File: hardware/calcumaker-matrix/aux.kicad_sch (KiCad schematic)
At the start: 1 part, among them J2 OLED 128x32 (DNP)

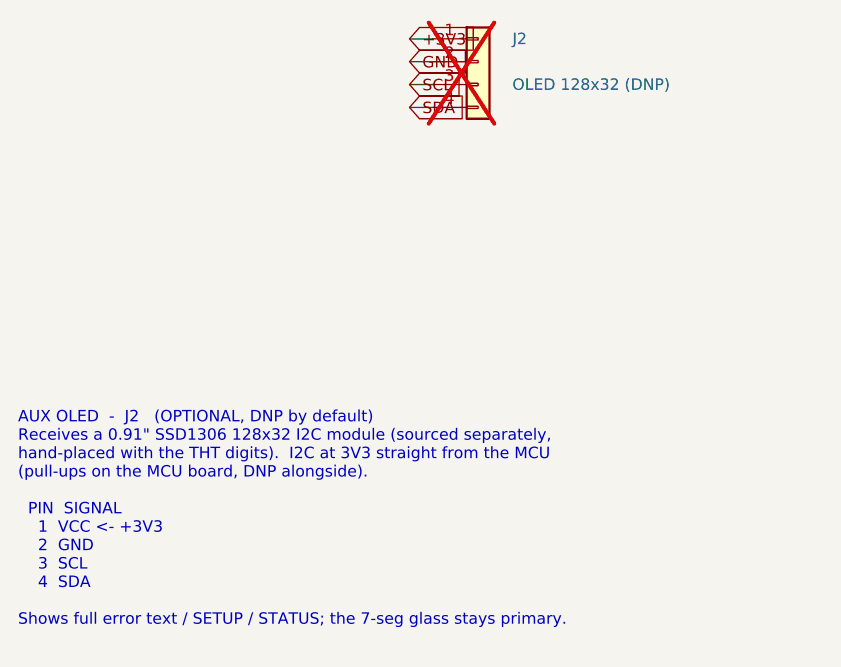
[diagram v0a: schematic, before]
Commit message: hardware: unified SPI display-module interface + RGB dot-matrix board
Make the display a swappable module on ONE technology-agnostic connector
(mirrors the keyboard-G0 pattern): the MCU board speaks a single SPI
"display intent" bus and each display board carries its own MCU that
renders locally. Two interchangeable modules on the same 12-pin FFC.

- calcumaker-matrix (NEW): full-color RGB dot matrix, 96x24 = 2304x 1mm
  XL-1010RGBC-2812B-S (C51900942) driven by an RP2040 (PIO). Nested
  multi-channel: led_cluster (8x8) x12 -> led_row (768px chain) x3.
  Dedicated VSYS LED-power inlet keeps amps off the signal FFC. Authored
  the 1mm 1010 footprint; RP2040/flash/shifter symbols are stock.
- calcumaker-display (7-seg): retrofit to a smart module -- added an
  STM32G031 SPI slave, and moved the 5V boost (TPS61022) + 74HCT125
  shifter off the MCU board onto it. Interconnect reworked CLK/DIN -> SPI.
- calcumaker-mcu: DisplayIF simplified to the unified SPI connector +
  a 2-pin VSYS outlet for the matrix LED rail.

Unified pinout (mcu J3 / display J1 / matrix J1): VSYS,VSYS,GND,GND,+3V3,
SPI_SCLK,SPI_MOSI,SPI_CS,DISP_IRQ,DISP_NRST,DISP_BOOT,GND.

All boards generate + check clean (mcu 46 / keyboard 179 / display 77 /
matrix 2339, no dup refs). Docs (PARTS.md, DESIGN.md, Makefile) updated.
Firmware is deferred; the SPI contract is documented so it is unblocked.

Co-Authored-By: Claude Opus 4.8 (1M context) <noreply@anthropic.com>
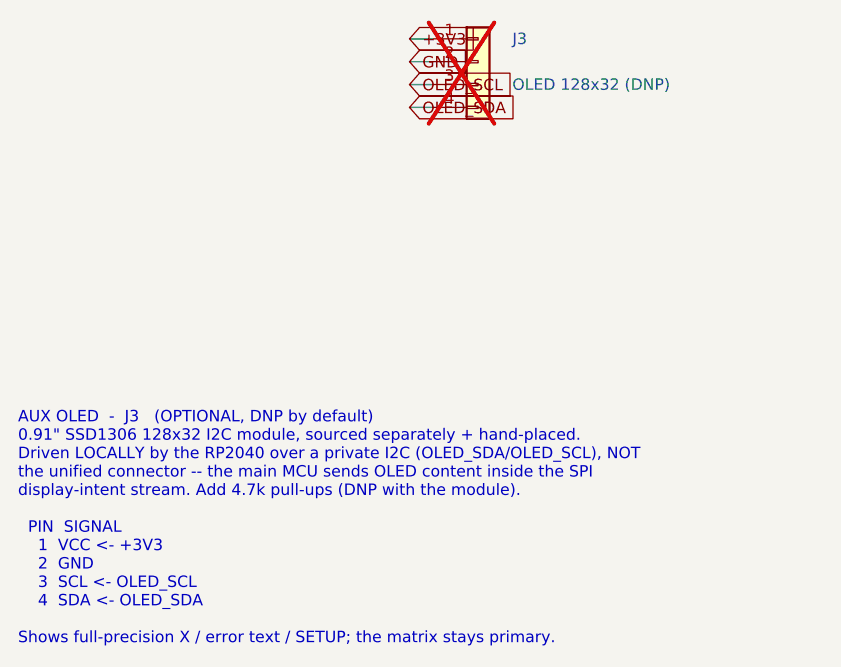
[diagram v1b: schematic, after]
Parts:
- removed J2: OLED 128x32 (DNP), Connector_PinHeader_2.54mm:PinHeader_1x04_P2.54mm_Vertical, symbol Connector_Generic:Conn_01x04
- added J3: OLED 128x32 (DNP), Connector_PinHeader_2.54mm:PinHeader_1x04_P2.54mm_Vertical, symbol Connector_Generic:Conn_01x04
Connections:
- net +3V3: now also J3.1 (Pin_1)
- net GND: now also J3.2 (Pin_2)
- new net OLED_SCL: J3.3 (Pin_3)
- new net OLED_SDA: J3.4 (Pin_4)
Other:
- note added: "AUX OLED - J3 (OPTIONAL, DNP by default) 0.91" SSD1306 128x32 I2C module, sourced separately + hand-placed. Driven LOCALLY by the RP2040 over a private I2C (OLED_SDA/OLED_SCL), NOT the unified connector -- the main MCU sends OLED content inside the SPI display-intent stream. Add 4.7k pull-ups (DNP with the module). PIN SIGNAL 1 VCC <- +3V3 2 GND 3 SCL <- OLED_SCL 4 SDA <- OLED_SDA Shows full-prec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"
- note removed: "AUX OLED - J2 (OPTIONAL, DNP by default) Receives a 0.91" SSD1306 128x32 I2C module (sourced separately, hand-placed with the THT digits). I2C at 3V3 straight from the MCU (pull-ups on the MCU board, DNP alongside). PIN SIGNAL 1 VCC <- +3V3 2 GND 3 SCL 4 SDA Shows full error text / SETUP / STATUS; the 7-seg glass stays primary."
- title: Calcumaker 16 — Display — Aux OLED 128x32 (SSD1306 I2C) — DNP-optional -> Calcumaker 16 — RGB Matrix — Aux OLED 128x32 (SSD1306 I2C) — DNP-optional
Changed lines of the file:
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@@
 	(paper "A3")
 	(title_block
-		(title "Calcumaker 16 — Display — Aux OLED 128x32 (SSD1306 I2C) — DNP-optional")
-		(date "2026-07-04")
-		(rev "0.2")
+		(title "Calcumaker 16 — RGB Matrix — Aux OLED 128x32 (SSD1306 I2C) — DNP-optional")
+		(date "2026-07-07")
+		(rev "0.1")
 		(company "calcumaker authors")
 	)
@@
 		(on_board yes)
 		(dnp yes)
-		(property "Reference" "J2"
+		(property "Reference" "J3"
 			(at 74.9300 68.5800 0)
 			(effects (font (size 1.27 1.27)) (justify left))
@@
 		(pin "4")
 		(instances
-			(project "calcumaker-display"
-				(path "/ca1c0000-0000-4000-8000-0000000d1501/ca1c0000-0000-4000-8000-0000000d1530"
-					(reference "J2")
+			(project "calcumaker-matrix"
+				(path "/ca1c0000-0000-4000-8000-0000000d3001/ca1c0000-0000-4000-8000-0000000d3230"
+					(reference "J3")
 					(unit 1)
 				)
@@
 		(stroke (width 0) (type default))
 	)
-	(global_label "SCL"
+	(global_label "OLED_SCL"
 		(shape input)
 		(at 63.5000 73.6600 180)
@@
 		(stroke (width 0) (type default))
 	)
-	(global_label "SDA"
+	(global_label "OLED_SDA"
 		(shape input)
 		(at 63.5000 76.2000 180)
@@
 		(effects (font (size 1.27 1.27)) (justify left))
 	)
-	(text "AUX OLED  -  J2   (OPTIONAL, DNP by default)\nReceives a 0.91\" SSD1306 128x32 I2C module (sourced separately,\nhand-placed with the THT digits).  I2C at 3V3 straight from the MCU\n(pull-ups on the MCU board, DNP alongside).\n\n  PIN  SIGNAL     \n    1  VCC <- +3V3\n    2  GND        \n    3  SCL        \n    4  SDA\n\nShows full error text / SETUP / STATUS; the 7-seg glass stays primary."
+	(text "AUX OLED  -  J3   (OPTIONAL, DNP by default)\n0.91\" SSD1306 128x32 I2C module, sourced separately + hand-placed.\nDriven LOCALLY by the RP2040 over a private I2C (OLED_SDA/OLED_SCL), NOT\nthe unified connector -- the main MCU sends OLED content inside the SPI\ndisplay-intent stream. Add 4.7k pull-ups (DNP with the module).\n\n  PIN  SIGNAL         \n    1  VCC <- +3V3    \n    2  GND            \n    3  SCL <- OLED_SCL\n    4  SDA <- OLED_SDA\n\nShows full-precision X / error text / SETUP; the matrix stays primary."
 		(exclude_from_sim no)
 		(at 20.00 110.00 0)
@@
 	(sheet_instances
 		(path "/"
-			(page "7")
+			(page "6")
 		)
 	)
